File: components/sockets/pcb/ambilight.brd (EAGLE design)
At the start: 69.2 x 54.7 mm, 12 parts, among them IC1 7805TV

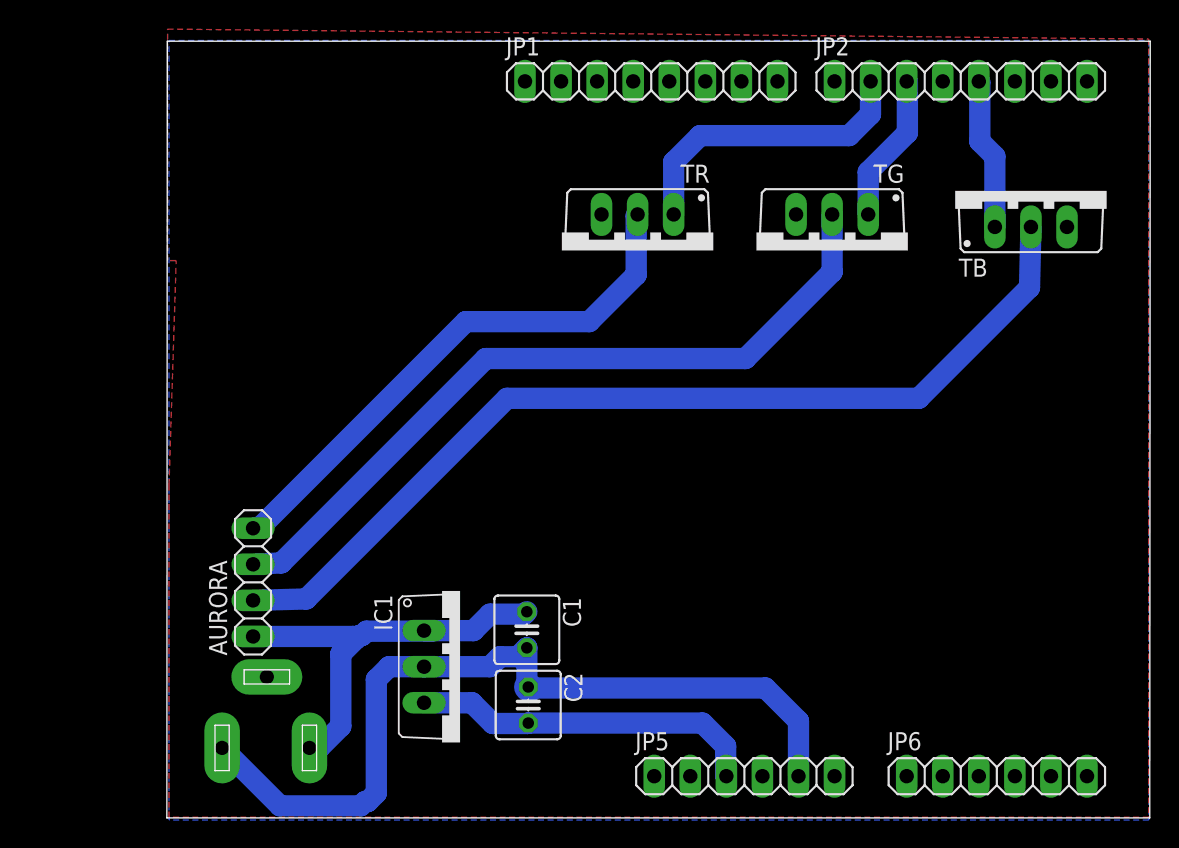
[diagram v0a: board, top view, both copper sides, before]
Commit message: Added Socket PCB, fixed ambilight sketch a bit
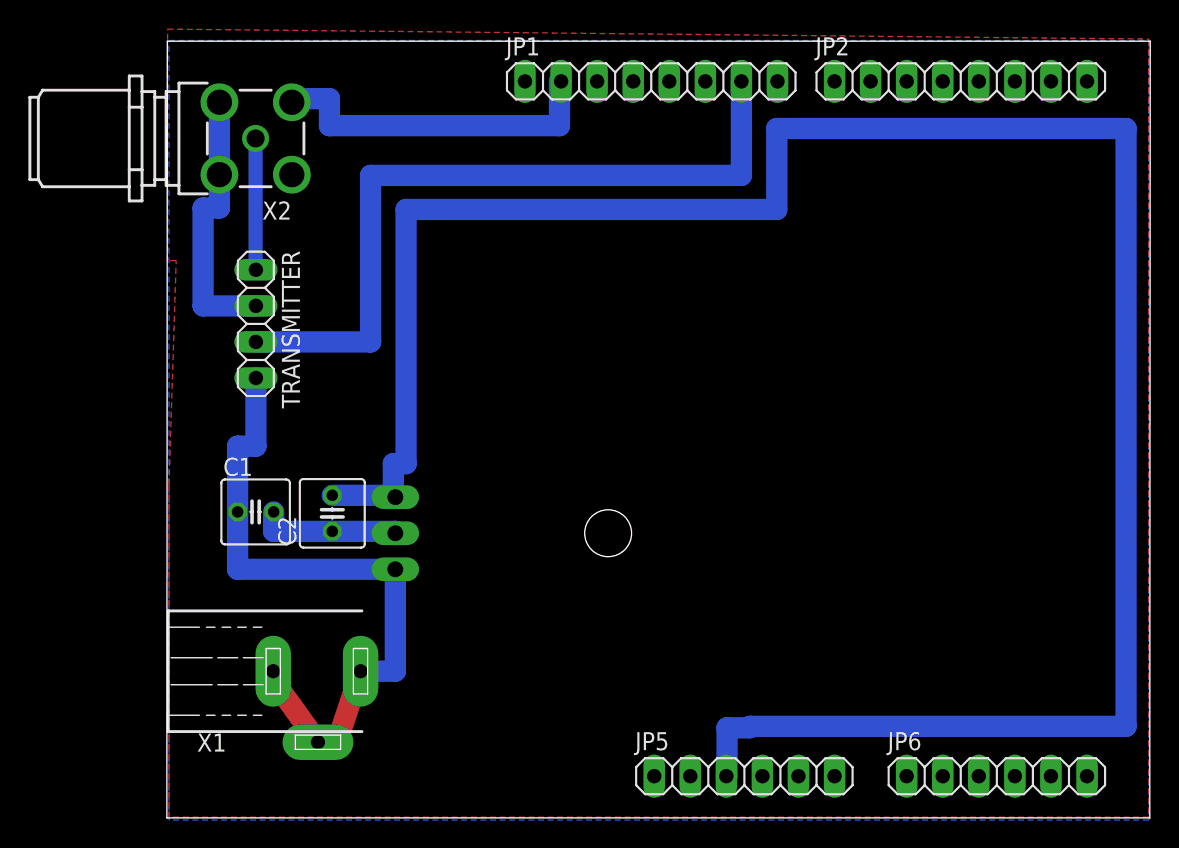
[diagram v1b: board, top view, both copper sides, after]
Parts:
- removed AURORA: (no value), pinhead:1X04
- removed TB, TG, TR: foo, transistor-power:TO220BV
- added TRANSMITTER: (no value), pinhead:1X04
- added X2: BU-SMA-G, con-coax:BU-SMA-G
- IC1: value 7805TV -> 7805T; device linear:TO220V -> linear:TO220H
- moved C1 20.8 mm to (36.7, 27.8), turned to 0 degrees
- moved C2 19.3 mm to (42.1, 27.7), turned to 90 degrees
- moved IC1 10.9 mm to (56.7, 26.3), flipped to the bottom, turned to 90 degrees
- moved X1 6.49 mm to (35.5, 16.6), flipped to the top, turned to 270 degrees
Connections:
- removed net N$10: JP2.2, TR.G
- removed net N$11: AURORA.4, TR.D
- removed net N$12: AURORA.3, TG.D
- removed net N$13: AURORA.2, TB.D
- removed net N$9: JP2.3, TG.G
- new net N$8: TRANSMITTER.1, X2.1
- net GND: now also JP1.2, TRANSMITTER.2, X2.2, X2.3, X2.4, X2.5; no longer JP5.5, TB.S, TG.S, TR.S
- net N$6: now also TRANSMITTER.4; no longer AURORA.1
- net N$7: now also JP1.7, TRANSMITTER.3; no longer JP2.5, TB.G
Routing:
- net N$4: track 24.7 -> 156.0 mm
- net N$13: track 68.0 -> 0.00 mm
- net N$12: track 53.3 -> 0.00 mm
- net N$7: track 10.7 -> 52.5 mm
- net N$11: track 38.6 -> 0.00 mm
- net N$10: track 21.3 -> 0.00 mm
- net N$6: track 30.1 -> 41.2 mm
- net N$9: track 10.5 -> 0.00 mm
- net N$8: track 0.00 -> 9.27 mm
